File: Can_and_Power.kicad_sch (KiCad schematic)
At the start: 11 parts, among them J1 776280-1, J4 776280-1, U4 ADM3057EBRWZ

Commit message: Digital IO, Relay, and Switchbox changes
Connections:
- net +12: now also J4.1; no longer J4.2
- net GND: now also J4.2; no longer J4.1
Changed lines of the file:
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@@
 	(wire
 		(pts
-			(xy 67.31 43.18) (xy 67.31 54.61)
+			(xy 67.31 41.91) (xy 67.31 54.61)
 		)
 		(stroke
@@
 	(symbol
 		(lib_id "power:VCC")
-		(at 67.31 43.18 0)
+		(at 60.96 43.18 0)
 		(unit 1)
 		(exclude_from_sim no)
@@
 		(fields_autoplaced yes)
 		(property "Reference" "#PWR012"
-			(at 67.31 46.99 0)
+			(at 60.96 46.99 0)
 			(effects
 				(font
@@
 		)
 		(property "Value" "+12"
-			(at 67.31 38.1 0)
+			(at 60.96 38.1 0)
 			(effects
 				(font
@@
 		)
 		(property "Footprint" ""
-			(at 67.31 43.18 0)
+			(at 60.96 43.18 0)
 			(effects
 				(font
@@
 		)
 		(property "Datasheet" ""
-			(at 67.31 43.18 0)
+			(at 60.96 43.18 0)
 			(effects
 				(font
@@
 		)
 		(property "Description" "Power symbol creates a global label with name \"VCC\""
-			(at 67.31 43.18 0)
+			(at 60.96 43.18 0)
 			(effects
 				(font
@@
 	(symbol
 		(lib_id "power:GND")
-		(at 60.96 43.18 180)
+		(at 67.31 41.91 180)
 		(unit 1)
 		(exclude_from_sim no)
@@
 		(fields_autoplaced yes)
 		(property "Reference" "#PWR010"
-			(at 60.96 36.83 0)
+			(at 67.31 35.56 0)
 			(effects
 				(font
@@
 		)
 		(property "Value" "GND"
-			(at 60.96 38.1 0)
+			(at 67.31 36.83 0)
 			(effects
 				(font
@@
 		)
 		(property "Footprint" ""
-			(at 60.96 43.18 0)
+			(at 67.31 41.91 0)
 			(effects
 				(font
@@
 		)
 		(property "Datasheet" ""
-			(at 60.96 43.18 0)
+			(at 67.31 41.91 0)
 			(effects
 				(font
@@
 		)
 		(property "Description" "Power symbol creates a global label with name \"GND\" , ground"
-			(at 60.96 43.18 0)
-			(effects
-				(font
+			(at 67.31 41.91 0)
+			(effects
+				(font

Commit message: Fixed ERC errors and warnings
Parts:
- U4: symbol 2025-07-12_07-19-05:ADM3057EBRWZ -> 2025-10-14_23-44-50:ADM3057EBRWZ
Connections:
- net CaNH: now also J1.3
- net CaNHi: no longer J1.3
- net CaNL: now also J1.4
- net CaNLi: no longer J1.4
- net GND: no longer J1.1, J4.2
- net +12 renamed +12V
- net +12V: now also J1.1; no longer J1.2
- net +3.3 renamed +3.3V
- net +5 renamed +5V
- new net GNDp: J1.2, J4.2
- no-connect marks 8 -> 9

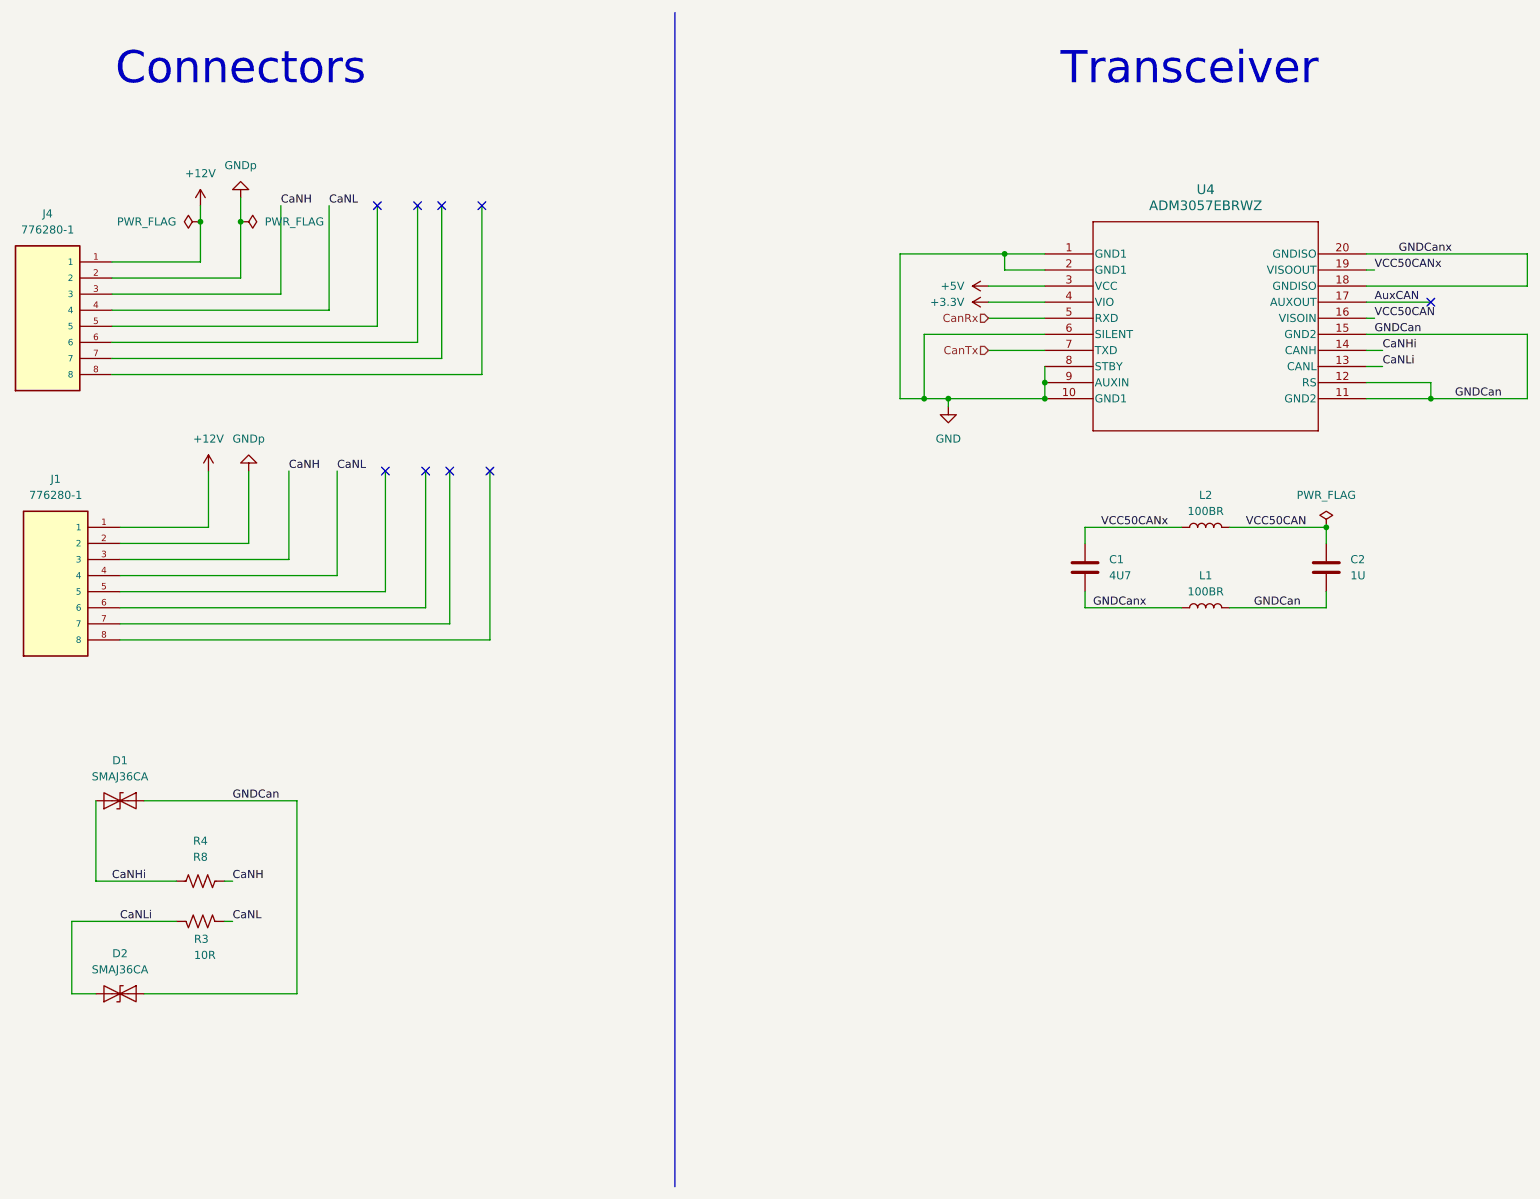
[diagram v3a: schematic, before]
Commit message: Moved everything to 23-POS AmpSeal
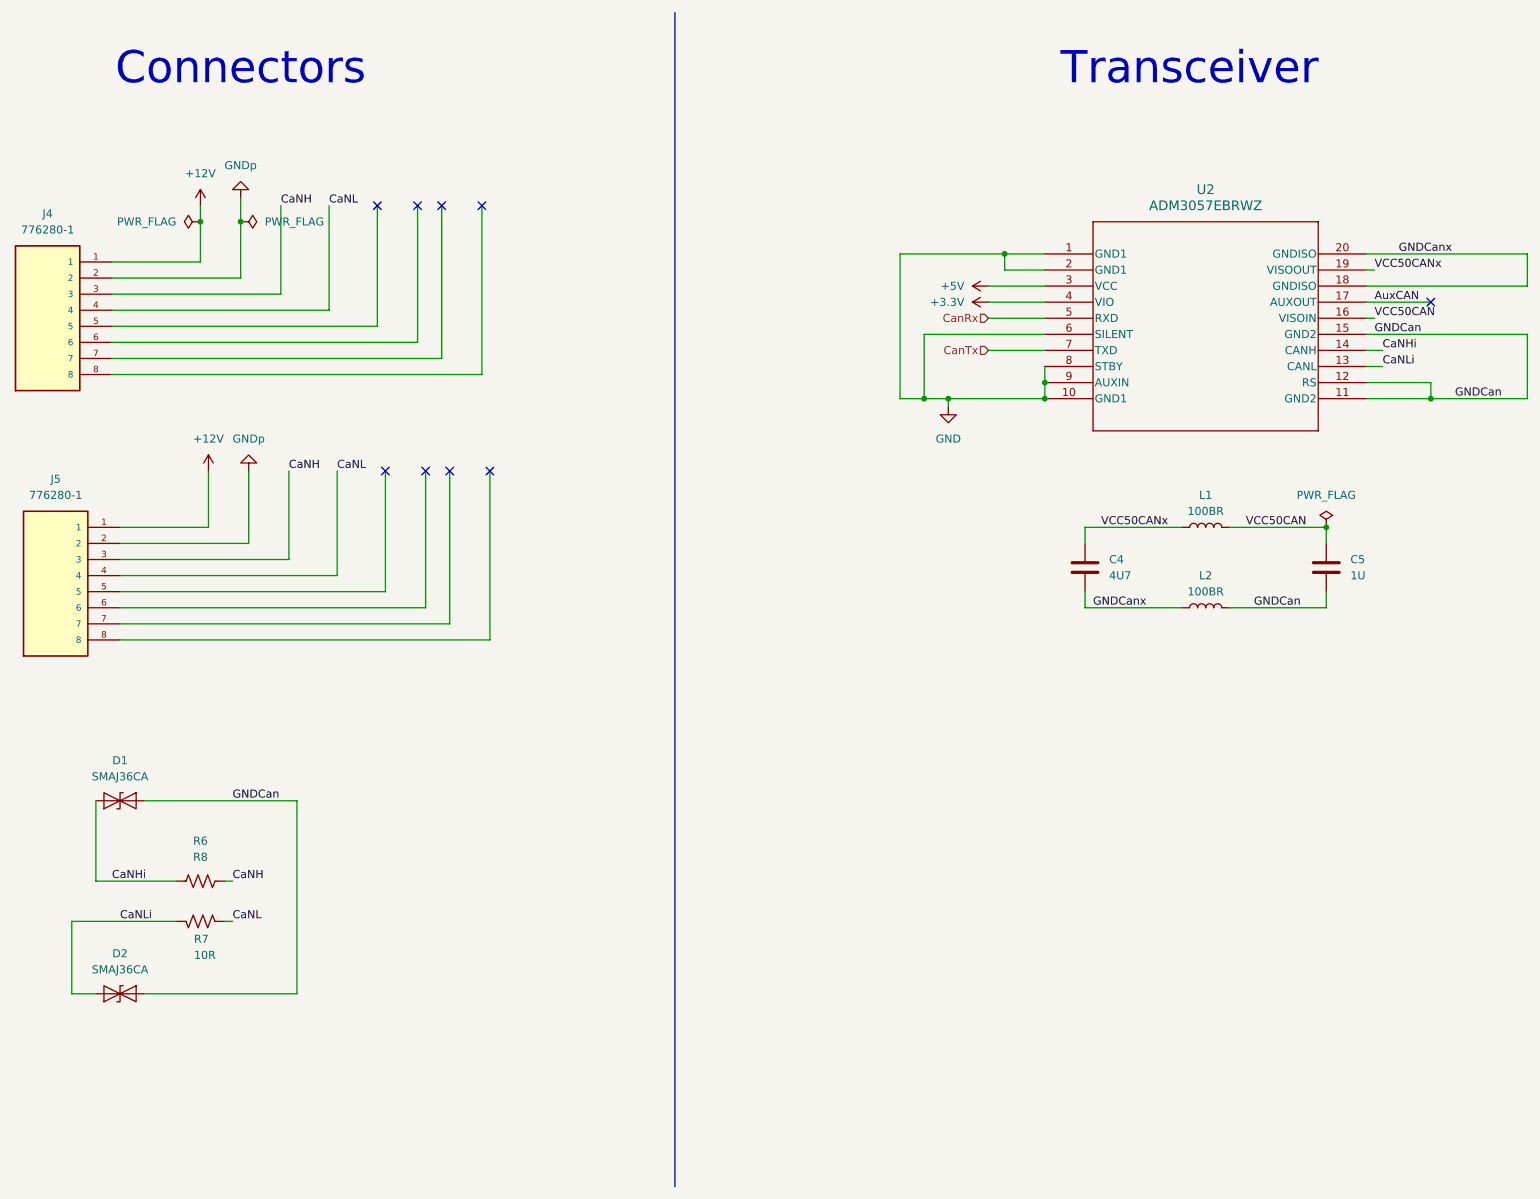
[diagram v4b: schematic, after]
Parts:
- renumbered C1 to C4, C2 to C5, J1 to J5, L2 to L1, L1 to L2, R4 to R6, R3 to R7, U4 to U2
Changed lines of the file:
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@@
 		(dnp no)
 		(fields_autoplaced yes)
-		(property "Reference" "#PWR02"
+		(property "Reference" "#PWR026"
 			(at 189.23 58.42 0)
 			(effects
@@
 		)
 		(instances
-			(project ""
-				(path "/c01682a2-308a-4674-9b8f-80e441c05d08/e5f6def6-a034-4879-9d0e-95711d983ac3"
-					(reference "#PWR02")
+			(project "Main-Board-V2"
+				(path "/c01682a2-308a-4674-9b8f-80e441c05d08/82598d9f-7302-484e-880f-c9b73897b20c"
+					(reference "#PWR026")
 					(unit 1)
 				)
@@
 		(dnp no)
 		(fields_autoplaced yes)
-		(property "Reference" "#PWR08"
+		(property "Reference" "#PWR020"
 			(at 60.96 46.99 0)
 			(effects
@@
 		)
 		(instances
-			(project ""
-				(path "/c01682a2-308a-4674-9b8f-80e441c05d08/e5f6def6-a034-4879-9d0e-95711d983ac3"
-					(reference "#PWR08")
+			(project "Main-Board-V2"
+				(path "/c01682a2-308a-4674-9b8f-80e441c05d08/82598d9f-7302-484e-880f-c9b73897b20c"
+					(reference "#PWR020")
 					(unit 1)
 				)
@@
 		(dnp no)
 		(fields_autoplaced yes)
-		(property "Reference" "#PWR01"
+		(property "Reference" "#PWR025"
 			(at 189.23 55.88 0)
 			(effects
@@
 		)
 		(instances
-			(project ""
-				(path "/c01682a2-308a-4674-9b8f-80e441c05d08/e5f6def6-a034-4879-9d0e-95711d983ac3"
-					(reference "#PWR01")
+			(project "Main-Board-V2"
+				(path "/c01682a2-308a-4674-9b8f-80e441c05d08/82598d9f-7302-484e-880f-c9b73897b20c"
+					(reference "#PWR025")
 					(unit 1)
 				)
@@
 		(dnp no)
 		(fields_autoplaced yes)
-		(property "Reference" "#FLG02"
+		(property "Reference" "#FLG03"
 			(at 69.215 45.72 0)
 			(effects
@@
 		)
 		(instances
-			(project ""
-				(path "/c01682a2-308a-4674-9b8f-80e441c05d08/e5f6def6-a034-4879-9d0e-95711d983ac3"
-					(reference "#FLG02")
+			(project "Main-Board-V2"
+				(path "/c01682a2-308a-4674-9b8f-80e441c05d08/82598d9f-7302-484e-880f-c9b73897b20c"
+					(reference "#FLG03")
 					(unit 1)
 				)
@@
 		(instances
 			(project "Main-Board-V2"
-				(path "/c01682a2-308a-4674-9b8f-80e441c05d08/e5f6def6-a034-4879-9d0e-95711d983ac3"
+				(path "/c01682a2-308a-4674-9b8f-80e441c05d08/82598d9f-7302-484e-880f-c9b73897b20c"
 					(reference "J4")
 					(unit 1)
@@
 		(dnp no)
 		(fields_autoplaced yes)
-		(property "Reference" "C2"
+		(property "Reference" "C5"
 			(at 242.57 99.0599 0)
 			(effects
@@
 		(instances
 			(project "Main-Board-V2"
-				(path "/c01682a2-308a-4674-9b8f-80e441c05d08/e5f6def6-a034-4879-9d0e-95711d983ac3"
-					(reference "C2")
+				(path "/c01682a2-308a-4674-9b8f-80e441c05d08/82598d9f-7302-484e-880f-c9b73897b20c"
+					(reference "C5")
 					(unit 1)
 				)
@@
 		)
 		(instances
-			(project ""
-				(path "/c01682a2-308a-4674-9b8f-80e441c05d08/e5f6def6-a034-4879-9d0e-95711d983ac3"
+			(project "Main-Board-V2"
+				(path "/c01682a2-308a-4674-9b8f-80e441c05d08/82598d9f-7302-484e-880f-c9b73897b20c"
 					(reference "#FLG04")
 					(unit 1)
@@
 		(dnp no)
 		(fields_autoplaced yes)
-		(property "Reference" "R4"
+		(property "Reference" "R6"
 			(at 60.96 143.51 90)
 			(effects
@@
 		(instances
 			(project "Main-Board-V2"
-				(path "/c01682a2-308a-4674-9b8f-80e441c05d08/e5f6def6-a034-4879-9d0e-95711d983ac3"
-					(reference "R4")
+				(path "/c01682a2-308a-4674-9b8f-80e441c05d08/82598d9f-7302-484e-880f-c9b73897b20c"
+					(reference "R6")
 					(unit 1)
 				)
@@
 		(instances
 			(project "Main-Board-V2"
-				(path "/c01682a2-308a-4674-9b8f-80e441c05d08/e5f6def6-a034-4879-9d0e-95711d983ac3"
+				(path "/c01682a2-308a-4674-9b8f-80e441c05d08/82598d9f-7302-484e-880f-c9b73897b20c"
 					(reference "D2")
 					(unit 1)
@@
 		(dnp no)
 		(fields_autoplaced yes)
-		(property "Reference" "#FLG01"
+		(property "Reference" "#FLG02"
 			(at 59.055 45.72 0)
 			(effects
@@
 		)
 		(instances
-			(project ""
-				(path "/c01682a2-308a-4674-9b8f-80e441c05d08/e5f6def6-a034-4879-9d0e-95711d983ac3"
-					(reference "#FLG01")
+			(project "Main-Board-V2"
+				(path "/c01682a2-308a-4674-9b8f-80e441c05d08/82598d9f-7302-484e-880f-c9b73897b20c"
+					(reference "#FLG02")
 					(unit 1)
 				)
@@
 		(dnp no)
 		(fields_autoplaced yes)
-		(property "Reference" "#PWR010"
+		(property "Reference" "#PWR022"
 			(at 67.31 35.56 0)
 			(effects
@@
 		(instances
 			(project "Main-Board-V2"
-				(path "/c01682a2-308a-4674-9b8f-80e441c05d08/e5f6def6-a034-4879-9d0e-95711d983ac3"
-					(reference "#PWR010")
+				(path "/c01682a2-308a-4674-9b8f-80e441c05d08/82598d9f-7302-484e-880f-c9b73897b20c"
+					(reference "#PWR022")
 					(unit 1)
 				)
@@
 		(on_board yes)
 		(dnp no)
-		(property "Reference" "J1"
+		(property "Reference" "J5"
 			(at 38.1 86.36 0)
 			(effects
@@
 		(instances
 			(project "Main-Board-V2"
-				(path "/c01682a2-308a-4674-9b8f-80e441c05d08/e5f6def6-a034-4879-9d0e-95711d983ac3"
-					(reference "J1")
+				(path "/c01682a2-308a-4674-9b8f-80e441c05d08/82598d9f-7302-484e-880f-c9b73897b20c"
+					(reference "J5")
 					(unit 1)
 				)
@@
 		(dnp no)
 		(fields_autoplaced yes)
-		(property "Reference" "U4"
+		(property "Reference" "U2"
 			(at 219.71 40.64 0)
 			(effects
@@
 		(instances
 			(project "Main-Board-V2"
-				(path "/c01682a2-308a-4674-9b8f-80e441c05d08/e5f6def6-a034-4879-9d0e-95711d983ac3"
-					(reference "U4")
+				(path "/c01682a2-308a-4674-9b8f-80e441c05d08/82598d9f-7302-484e-880f-c9b73897b20c"
+					(reference "U2")
 					(unit 1)
 				)
@@
 		(on_board yes)
 		(dnp no)
-		(property "Reference" "R3"
+		(property "Reference" "R7"
 			(at 59.944 159.004 90)
 			(effects
@@
 		(instances
 			(project "Main-Board-V2"
-				(path "/c01682a2-308a-4674-9b8f-80e441c05d08/e5f6def6-a034-4879-9d0e-95711d983ac3"
-					(reference "R3")
+				(path "/c01682a2-308a-4674-9b8f-80e441c05d08/82598d9f-7302-484e-880f-c9b73897b20c"
+					(reference "R7")
 					(unit 1)
 				)
@@
 		(dnp no)
 		(fields_autoplaced yes)
-		(property "Reference" "#PWR07"
+		(property "Reference" "#PWR021"
 			(at 62.23 88.9 0)
 			(effects
@@
 		)
 		(instances
-			(project ""
-				(path "/c01682a2-308a-4674-9b8f-80e441c05d08/e5f6def6-a034-4879-9d0e-95711d983ac3"
-					(reference "#PWR07")
+			(project "Main-Board-V2"
+				(path "/c01682a2-308a-4674-9b8f-80e441c05d08/82598d9f-7302-484e-880f-c9b73897b20c"
+					(reference "#PWR021")
 					(unit 1)
 				)
@@
 		(dnp no)
 		(fields_autoplaced yes)
-		(property "Reference" "#PWR06"
+		(property "Reference" "#PWR023"
 			(at 68.58 78.74 0)
 			(effects
@@
 		(instances
 			(project "Main-Board-V2"
-				(path "/c01682a2-308a-4674-9b8f-80e441c05d08/e5f6def6-a034-4879-9d0e-95711d983ac3"
-					(reference "#PWR06")
+				(path "/c01682a2-308a-4674-9b8f-80e441c05d08/82598d9f-7302-484e-880f-c9b73897b20c"
+					(reference "#PWR023")
 					(unit 1)
 				)
@@
 		(dnp no)
 		(fields_autoplaced yes)
-		(property "Reference" "#PWR05"
+		(property "Reference" "#PWR024"
 			(at 179.07 81.28 0)
 			(effects
@@
 		(instances
 			(project "Main-Board-V2"
-				(path "/c01682a2-308a-4674-9b8f-80e441c05d08/e5f6def6-a034-4879-9d0e-95711d983ac3"
-					(reference "#PWR05")
+				(path "/c01682a2-308a-4674-9b8f-80e441c05d08/82598d9f-7302-484e-880f-c9b73897b20c"
+					(reference "#PWR024")
 					(unit 1)
 				)
@@
 		(instances
 			(project "Main-Board-V2"
-				(path "/c01682a2-308a-4674-9b8f-80e441c05d08/e5f6def6-a034-4879-9d0e-95711d983ac3"
+				(path "/c01682a2-308a-4674-9b8f-80e441c05d08/82598d9f-7302-484e-880f-c9b73897b20c"
 					(reference "D1")
 					(unit 1)
@@
 		(dnp no)
 		(fields_autoplaced yes)
-		(property "Reference" "C1"
+		(property "Reference" "C4"
 			(at 204.47 99.0599 0)
 			(effects
@@
 		(instances
 			(project "Main-Board-V2"
-				(path "/c01682a2-308a-4674-9b8f-80e441c05d08/e5f6def6-a034-4879-9d0e-95711d983ac3"
-					(reference "C1")
+				(path "/c01682a2-308a-4674-9b8f-80e441c05d08/82598d9f-7302-484e-880f-c9b73897b20c"
+					(reference "C4")
 					(unit 1)
 				)
@@
 		(dnp no)
 		(fields_autoplaced yes)
-		(property "Reference" "L2"
+		(property "Reference" "L1"
 			(at 219.71 88.9 90)
 			(effects
@@
 		(instances
 			(project "Main-Board-V2"
-				(path "/c01682a2-308a-4674-9b8f-80e441c05d08/e5f6def6-a034-4879-9d0e-95711d983ac3"
-					(reference "L2")
+				(path "/c01682a2-308a-4674-9b8f-80e441c05d08/82598d9f-7302-484e-880f-c9b73897b20c"
+					(reference "L1")
 					(unit 1)
 				)
@@
 		(dnp no)
 		(fields_autoplaced yes)
-		(property "Reference" "L1"
+		(property "Reference" "L2"
 			(at 219.71 101.6 90)
 			(effects
@@
 		(instances
 			(project "Main-Board-V2"
-				(path "/c01682a2-308a-4674-9b8f-80e441c05d08/e5f6def6-a034-4879-9d0e-95711d983ac3"
-					(reference "L1")
-					(unit 1)
-				)
+				(path "/c01682a2-308a-4674-9b8f-80e441c05d08/82598d9f-7302-484e-880f-c9b73897b20c"
+					(reference "L2")
+					(unit 1)
+				)

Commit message: Idk what but it is better than before
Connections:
- net at J4.5: now also J5.5
- net at J4.6: now also J5.6
- net at J4.7: now also J5.7
- net at J4.8: now also J5.8
- no-connect marks 9 -> 1
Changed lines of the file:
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@@
-	)
-	(no_connect
-		(at 96.52 85.09)
-	)
-	(no_connect
-		(at 88.9 43.18)
-	)
-	(no_connect
-		(at 105.41 43.18)
 	)
 	(no_connect
 		(at 255.27 58.42)
 	)
-	(no_connect
-		(at 99.06 43.18)
-	)
-	(no_connect
-		(at 90.17 85.09)
-	)
-	(no_connect
-		(at 100.33 85.09)
-	)
-	(no_connect
-		(at 106.68 85.09)
-	)
-	(no_connect
-		(at 95.25 43.18)
-	)
 	(wire
 		(pts
@@
 	(wire
 		(pts
-			(xy 106.68 85.09) (xy 106.68 111.76)
+			(xy 106.68 69.85) (xy 106.68 111.76)
 		)
 		(stroke
@@
 	(wire
 		(pts
+			(xy 100.33 67.31) (xy 100.33 109.22)
+		)
+		(stroke
+			(width 0)
+			(type default)
+		)
+	)
+	(wire
+		(pts
 			(xy 73.66 43.18) (xy 73.66 57.15)
 		)
@@
 	(wire
 		(pts
-			(xy 95.25 43.18) (xy 95.25 64.77)
-		)
-		(stroke
-			(width 0)
-			(type default)
-		)
-	)
-	(wire
-		(pts
 			(xy 171.45 73.66) (xy 171.45 50.8)
 		)
@@
 	(wire
 		(pts
-			(xy 88.9 43.18) (xy 88.9 62.23)
-		)
-		(stroke
-			(width 0)
-			(type default)
-		)
-	)
-	(wire
-		(pts
 			(xy 60.96 43.18) (xy 60.96 45.72)
 		)
@@
 	(wire
 		(pts
-			(xy 46.99 64.77) (xy 95.25 64.77)
-		)
-		(stroke
-			(width 0)
-			(type default)
-		)
-	)
-	(wire
-		(pts
-			(xy 99.06 43.18) (xy 99.06 67.31)
+			(xy 46.99 64.77) (xy 96.52 64.77)
 		)
 		(stroke
@@
 	(wire
 		(pts
-			(xy 90.17 85.09) (xy 90.17 104.14)
-		)
-		(stroke
-			(width 0)
-			(type default)
-		)
-	)
-	(wire
-		(pts
-			(xy 105.41 43.18) (xy 105.41 69.85)
+			(xy 90.17 62.23) (xy 90.17 104.14)
 		)
 		(stroke
@@
 	(wire
 		(pts
-			(xy 96.52 85.09) (xy 96.52 106.68)
+			(xy 96.52 64.77) (xy 96.52 106.68)
 		)
 		(stroke
@@
 	(wire
 		(pts
-			(xy 46.99 67.31) (xy 99.06 67.31)
+			(xy 46.99 67.31) (xy 100.33 67.31)
 		)
 		(stroke
@@
 	(wire
 		(pts
-			(xy 46.99 62.23) (xy 88.9 62.23)
+			(xy 46.99 62.23) (xy 90.17 62.23)
 		)
 		(stroke
@@
 	(wire
 		(pts
-			(xy 100.33 85.09) (xy 100.33 109.22)
-		)
-		(stroke
-			(width 0)
-			(type default)
-		)
-	)
-	(wire
-		(pts
 			(xy 200.66 106.68) (xy 200.66 104.14)
 		)
@@
 	(wire
 		(pts
-			(xy 46.99 69.85) (xy 105.41 69.85)
-		)
-		(stroke
+			(xy 46.99 69.85) (xy 106.68 69.85)
+		)
+		(stroke
